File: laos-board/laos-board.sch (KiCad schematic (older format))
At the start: 88 parts, among them P1 POWER, P10 XY_LIMIT, P11 OUTPUTS, P12 VIN, P2 Z, P3 Y, P4 X, P5 LASER, P7 I2C, P8 ANALOG, P8 CAN, P9 Z_LIMIT, U1 POLOLU1201, U2 MAGJACK, U2 POLOLU1201, U3 POLOLU1201, U4 65HVD251, U4 7805, X1 USB-A-H

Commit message: more dataheets, rev2 of board design
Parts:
- removed R15, R17, R19, R21: 5K, symbol R
- removed SD1: SDCARD, symbol CONN_6
- added C6: 100nF, symbol C
- added P14: Vsensor, symbol CONN_2
- added P? (x14): CONN_1, symbol CONN_1
- added U5: SDCARD, symbol SDCARD
- P10: value XY_LIMIT -> XYLIMIT
- P9: value Z_LIMIT -> ZLIMIT
- gave numbers to parts that had none: 2
- renumbered 6 to OC6, U2 to U10, U4 to U6
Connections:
- net labels added: VAA
- wire segments 261 -> 276
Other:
- note added: "2"
- note added: "Keep Ethernet lines short, close and equal length"
- note added: "SJ0"
- note added: "SJ5A"
- note added: "SJ5B"
- note added: "SJ6A"
- note added: "SJ6B"
- note added: "SJ8"
- note added: "SJ9"
- note added: "Solder joint 0: 5V from USB\nSolder joint 1: 5V from VIN\nSolder joint 5: Sensor voltage 5V\nSolder joint 9: Sensor voltage VIN\nSolder joint 6: Motor voltage 5V \nSolder joint 8: Motor voltage VIN\n"
- note removed: "1"
- note removed: "Solder Joint 1\nConnect if USB not connected to PC"
- moved on the sheet: P7, P8, R16, R18, R20, R22

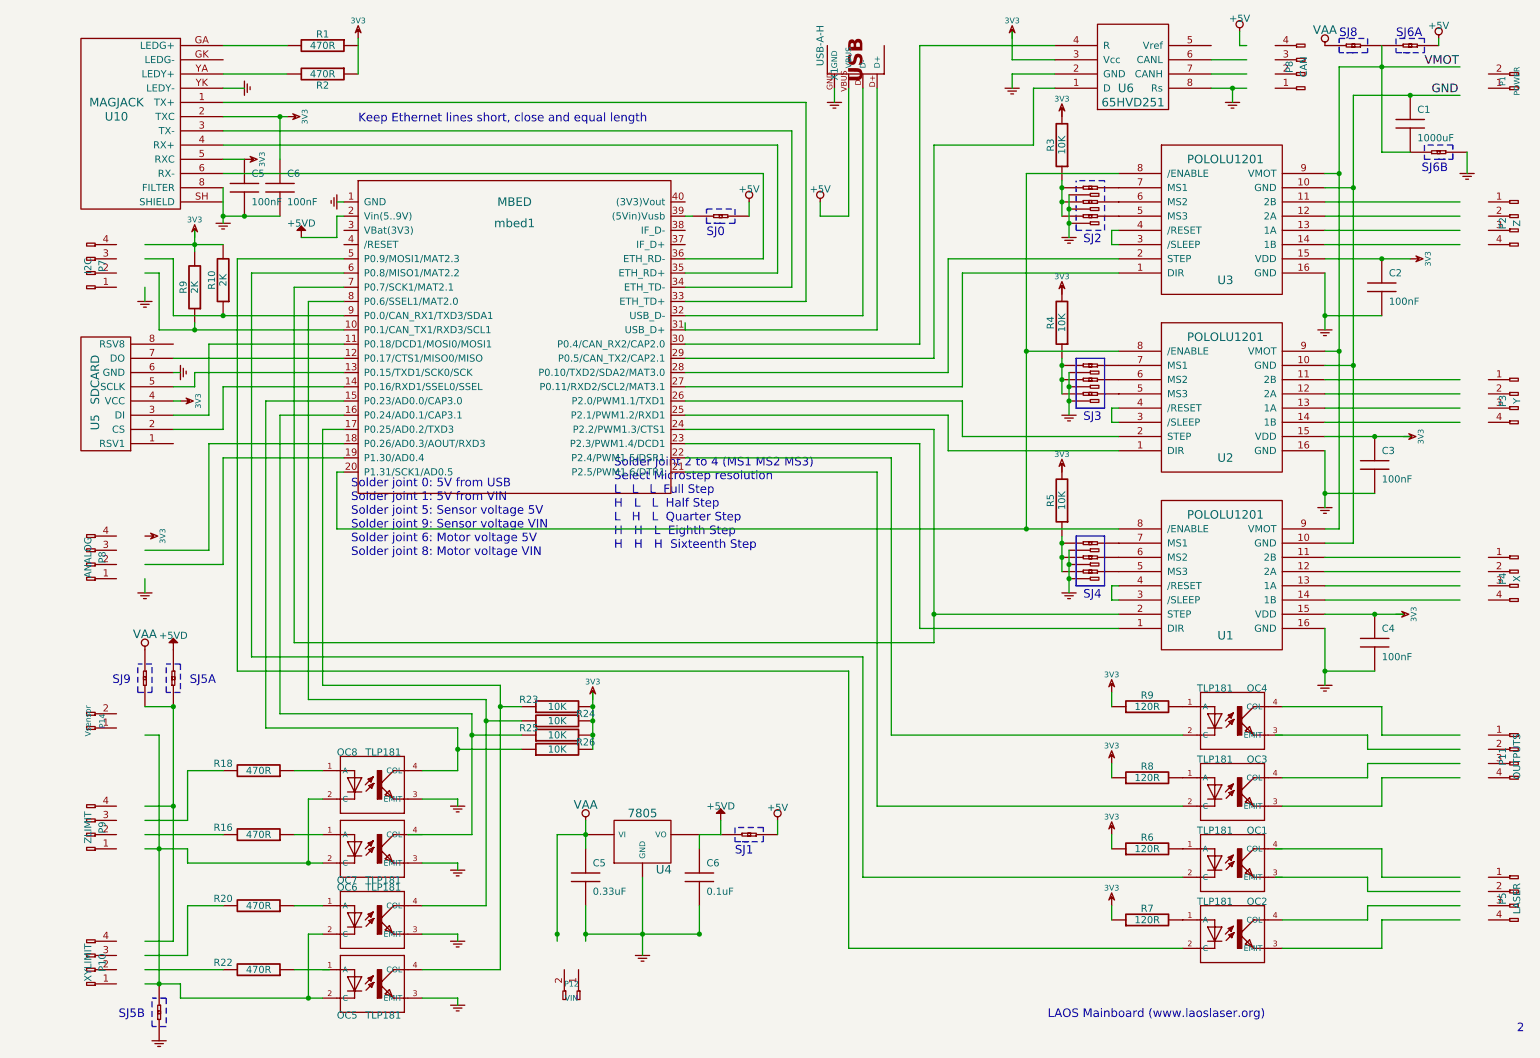
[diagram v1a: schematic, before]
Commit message: simplified schematics Added info on board layout and connector placement
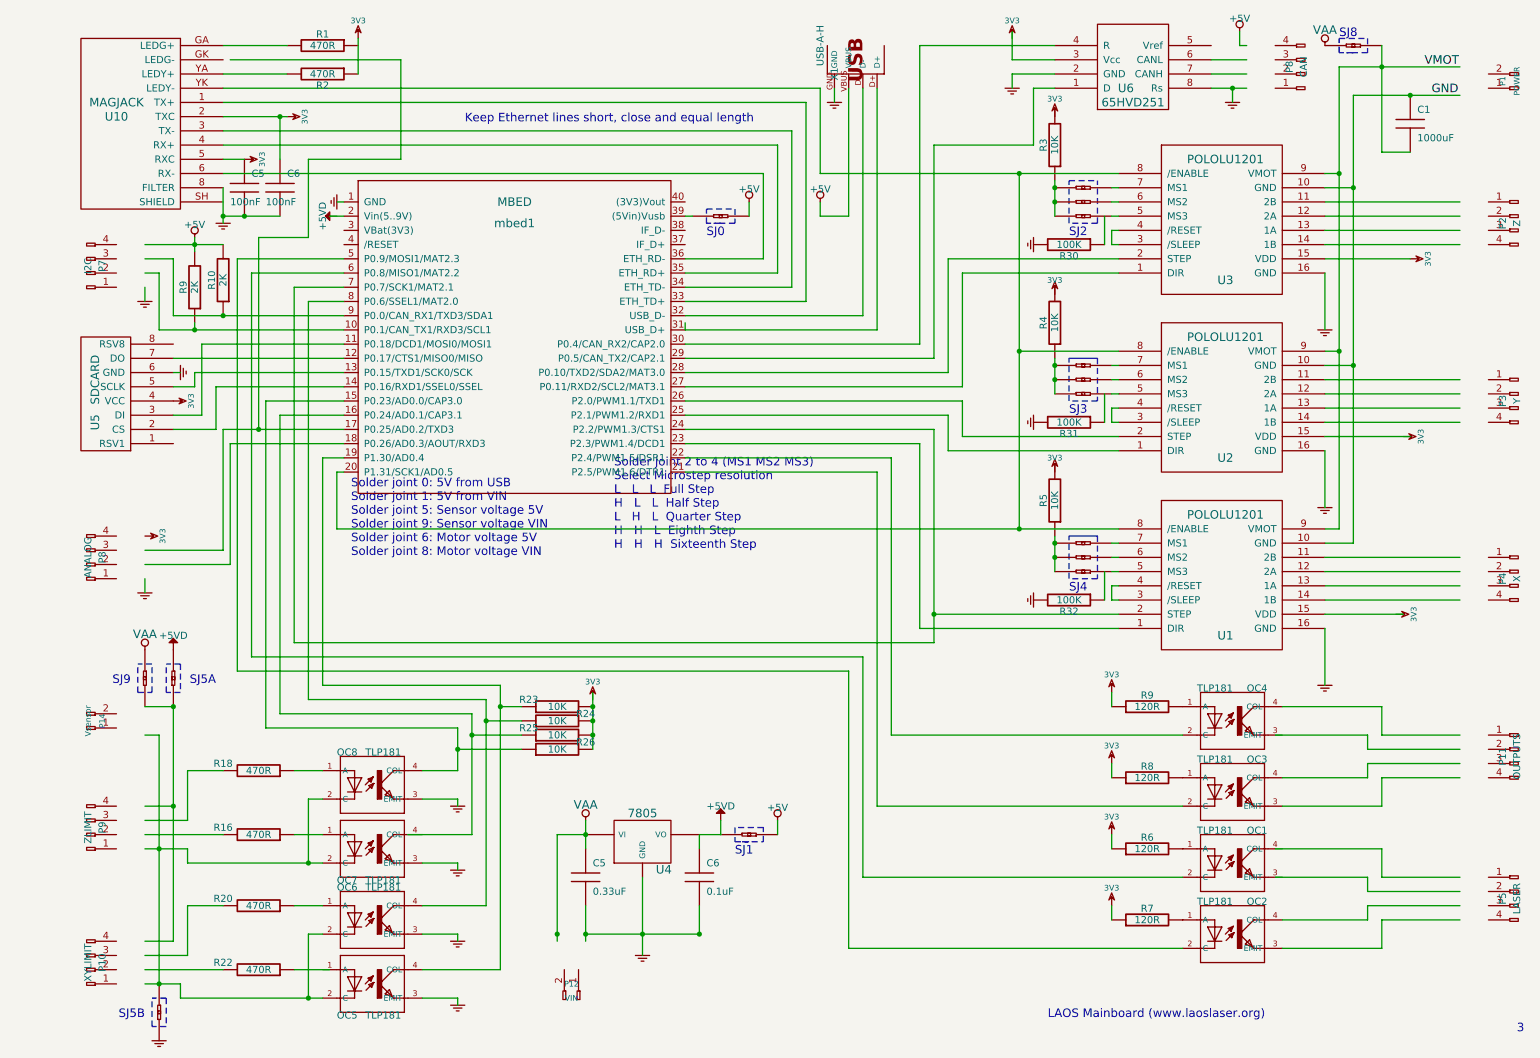
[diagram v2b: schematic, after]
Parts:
- removed C2, C3, C4: 100nF, symbol C
- removed P? (x4), SJ1A? (x9): CONN_1, symbol CONN_1
- added R30, R31, R32: 100K, symbol R
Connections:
- wire segments 276 -> 284
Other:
- note added: "3"
- note removed: "2"
- note removed: "SJ6A"
- note removed: "SJ6B"
- moved on the sheet: R3, R4, R5

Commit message: Add laos-board revision 2 schematics
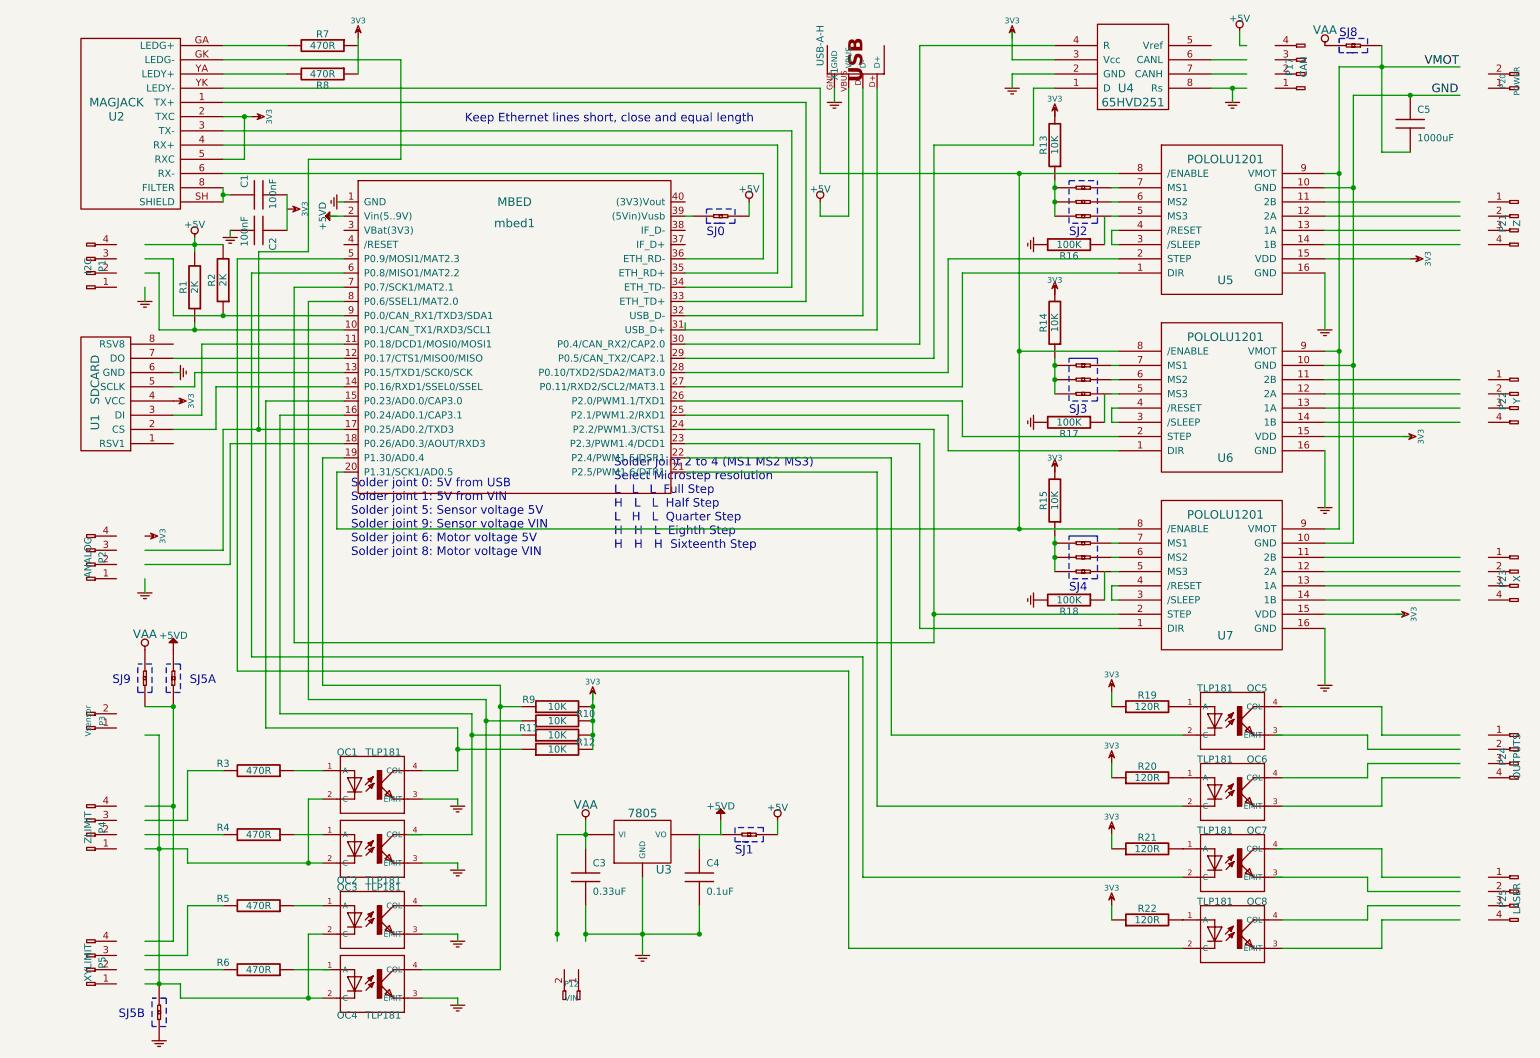
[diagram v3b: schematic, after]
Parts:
- gave numbers to parts that had none: 27
- renumbered C6 to C1, C5 to C2, C5 to C3, C6 to C4, C1 to C5, OC8 to OC1, OC7 to OC2, OC6 to OC3, OC5 to OC4, OC4 to OC5, OC3 to OC6, OC1 to OC7, OC2 to OC8, P7 to P1, P8 to P17, P8 to P2, P1 to P20, P2 to P21, P3 to P22, P4 to P23, P11 to P24, P5 to P25, P14 to P3, P9 to P4, P10 to P5, R9 to R1, R24 to R10, R25 to R11, R26 to R12, R3 to R13, R4 to R14, R5 to R15, R30 to R16, R31 to R17, R32 to R18, R9 to R19, R10 to R2, R8 to R20, R6 to R21, R7 to R22, R18 to R3, R16 to R4, R20 to R5, R22 to R6, R1 to R7, R2 to R8, R23 to R9, SJ1A to SJ1A10, SJ2A to SJ2A1, SJ3A to SJ3A1, U5 to U1, U10 to U2, U4 to U3, U6 to U4, U3 to U5, U2 to U6, U1 to U7
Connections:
- wire segments 284 -> 286
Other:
- note removed: "3"
- note removed: "LAOS Mainboard (www.laoslaser.org)"
- moved on the sheet: C1, C2
